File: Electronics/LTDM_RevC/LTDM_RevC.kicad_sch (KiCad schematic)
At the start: 182 parts, among them J1 Conn_01x03_Male, J11 CSR_Bypass, J12 SpringTerminal, J13 Ban1, J14 CSR_Bypass, J15 SpringTerminal, J16 Barrel_Jack, J17 Ban2, J18 Conn_01x03_Male, J2 Conn_01x03_Male, J22 Barrel_Jack, J25 Ban3, J26 Conn_01x03_Male, J29 Conn_01x03_Male, J31 Conn_01x03_Male, J32 Conn_01x03_Male, J4 Conn_01x03_Male, J5 Conn_02x15_Odd_Even, J6 Conn_01x03_Male, J7 Conn_01x04_Socket, J9 Conn_01x03_Male, Q5 FQP27P06, Q6 IRLZ44N, SW3 SW_DPST, U1 74LVC1G11, U10 AP64501SP, U15 LM393, U17 OPA2350, U20 74AUC2G86, U26 74LVC1G11, U3 OPA2350, U31 74LVC1G11, U32 74LVC1G11, U5 LM393, U7 Teensy4.1A, U8 Teensy4.1B

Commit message: Improved  and characterized ADC sample time
Previously took ~6.3uS to sample both ADCs but have gotten it down to a sweet ~3.4uS by disabling 'long sampling mode' and ADC_CFG_ADSTS(3) to ADC_CFG_ADSTS(0). Apparently that was upping sample time.

This arrangement is likely noisier but gives a user an extra 3.5uS to play with in render()

This is for 600MHz.

Trimming away old code too :)
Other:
- sheet String_Drivers_GD1 ports: added STRING1-; removed STRING-
- note removed: "Improvements to Rev B boards: ☑ Change OPA350 to OPA2350 - now has correct pinout and is slightly cheaper ☑ Fixed polarity of dc barrel jacks ☑ Reverse polarity protection(!!) ☑ Rearrange pinout to use FlexPWM output directly (going to have to perform some surgery on current board to verify a correct pinout). -On that note, add a dev board style pinheader breakout to give access to unused pins. W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"
- note removed: "change log: -removed connection between Pin 2<->9 and 3<->10 -- 9 & 10 were hardware interrupts, but changed to use software interrupts - preamplifier used to have balanced gain of 22.28 per stage for total of ~496, but now the first stage has more gain and the second less - to incorporate the S+H and have a slightly hotter output from the S+H -5V regulator - is switch-controlled rather than jump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"
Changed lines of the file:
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@@
 	(text "Ongoing questions:\n- reconsidering the idea of shunting the current out of the resistor"
 		(exclude_from_sim no)
-		(at -37.084 -11.176 0)
+		(at 11.43 7.112 0)
 		(effects
 			(font
@@
 		)
 	)
-	(text "change log:\n\n-removed connection between Pin 2<->9 and 3<->10 -- 9 & 10 were hardware interrupts, but changed to use software interrupts\n\n- preamplifier used to have balanced gain of 22.28 per stage for total of ~496, but now the first stage has more gain and the second less\n	- to incorporate the S+H and have a slightly hotter output from the S+H\n\n-5V regulator\n	- is switch-controlled rather than jumper controlled\n	- higher performance buck converter rather linear 7805\n\n- dissipating resistor changed from  680Ohm (1/4W) to 100Ohm (5W). Better dissipation of ringing.\n\n- Removed potentiometers from precision rectifiers - instead relying on 0.1% thin film resistors"
-		(exclude_from_sim no)
-		(at 181.864 -17.526 0)
-		(effects
-			(font
-				(size 1.27 1.27)
-			)
-			(justify left)
-		)
-	)
 	(text "Key:\nSW = switch (8)\nBT = button (8)\nFP = footpedal (2)\nSL = Slide Pot (8)\nRV = potentiometer (8)"
 		(exclude_from_sim no)
@@
 		)
 	)
-	(text "Improvements to Rev B boards:\n☑ Change OPA350 to OPA2350 - now has correct pinout and is slightly cheaper\n☑ Fixed polarity of dc barrel jacks\n☑ Reverse polarity protection(!!)\n☑ Rearrange pinout to use FlexPWM output directly (going to have to perform some surgery on current board to verify a correct pinout).\n-On that note, add a dev board style pinheader breakout to give access to unused pins. Will be nice if I try to do any LED aliasing experiments --> NVM - using most pins already :)\n-move onboard 5V regulator jumper - too hard to reach currently when switching between teensy power over USB vs powered by 12V supply  (maybe replace with a small switch??)\n-mounting holes for Heat sink leads. (Planning to only use the TO-220-2 package resistors now bc of easy value swapping and easy heatsinking)\n☑ PCB mount 1/4” TRS Expression Pedal plugs (at least two). Maybe panel mount instead incase we want to make an enclosure for this board.\n\nStretch goals, though this might be getting beyond “just a few minor changes”\n-add an FX insert between string sense and teensy analog in for experimenting with pedals in the loop. Nice linear buffered output and input.\n-Small current-sense resistor before string is terminated to ground for measuring current with scope. Will be nice for string comparison analysis.\n-Add sample-and-hold (need to figure out the most appropriate spot for this), but this will be necessary for FX send/return anyway. Makes it possible to monitor/record/listen/add effects to a direct audio output rather than just relying on microphone, acoustic output, or piezo pickups. I’m very interested to hear what this sounds like and if it can be used to sound good.\n-Move analog switch - it needs to be able to switch the analogRead()’s input to come pre or post FX insert. This would be so we can switch between active sustaining with FX and active damping.\n-Adjustable string sense input gain with a trim pot might be nice - we’re occasionally clipping the input when a string really gets moving hard or we use stronger magnets.\n-Any leftover GPIO would be nice to throw some DIP switches or tactile buttons to for further devboard-iness\n-Add a current sense bit\n- Shift S&H to go between gain blocks"
-		(exclude_from_sim no)
-		(at 22.86 -62.23 0)
-		(effects
-			(font
-				(size 1.27 1.27)
-			)
-			(justify left)
-		)
-	)
 	(text "Excluding these because the true gate drivers are better (I think...)\nProperties:\n[X] Exclude from board (to exclude from board)\n[X] Do not populate (for the visual)\n\ncould be cheaper alternative to proper gate drivers"
 		(exclude_from_sim no)
@@
 		)
 		(instances
-			(project "Lorentz_TDM_RevB_V2"
+			(project "LTDM_RevC"
 				(path "/21bd285d-c5a5-466d-bf8a-edfa6cbb8182"
 					(page "7")
@@
 		)
 		(instances
-			(project "Lorentz_TDM_RevB_V2"
+			(project "LTDM_RevC"
 				(path "/21bd285d-c5a5-466d-bf8a-edfa6cbb8182"
 					(page "7")
@@
 			)
 		)
-		(pin "STRING-" output
+		(pin "STRING1-" output
 			(at 511.81 120.65 0)
 			(effects
@@
 		)
 		(instances
-			(project "Lorentz_TDM_RevB_V2"
+			(project "LTDM_RevC"
 				(path "/21bd285d-c5a5-466d-bf8a-edfa6cbb8182"
 					(page "8")
@@
 		)
 		(instances
-			(project "Lorentz_TDM_RevB_V2"
+			(project "LTDM_RevC"
 				(path "/21bd285d-c5a5-466d-bf8a-edfa6cbb8182"
 					(page "6")
@@
 		)
 		(instances
-			(project "Lorentz_TDM_RevB_V2"
+			(project "LTDM_RevC"
 				(path "/21bd285d-c5a5-466d-bf8a-edfa6cbb8182"
 					(page "3")
@@
 		)
 		(instances
-			(project "Lorentz_TDM_RevB_V2"
+			(project "LTDM_RevC"
 				(path "/21bd285d-c5a5-466d-bf8a-edfa6cbb8182"
 					(page "2")
@@
 		)
 		(instances
-			(project "Lorentz_TDM_RevB_V2"
+			(project "LTDM_RevC"
 				(path "/21bd285d-c5a5-466d-bf8a-edfa6cbb8182"
 					(page "5")

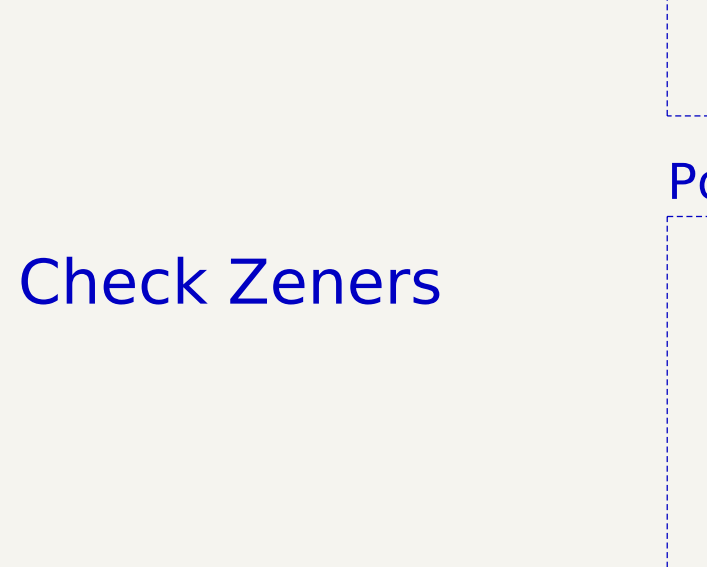
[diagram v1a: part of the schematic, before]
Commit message: Channel 2 fixed!
Channel 2 now working again
Now you can enable/disable RMS limiting and noise
LEDs indicate settings (refer to visualguide.jpg)
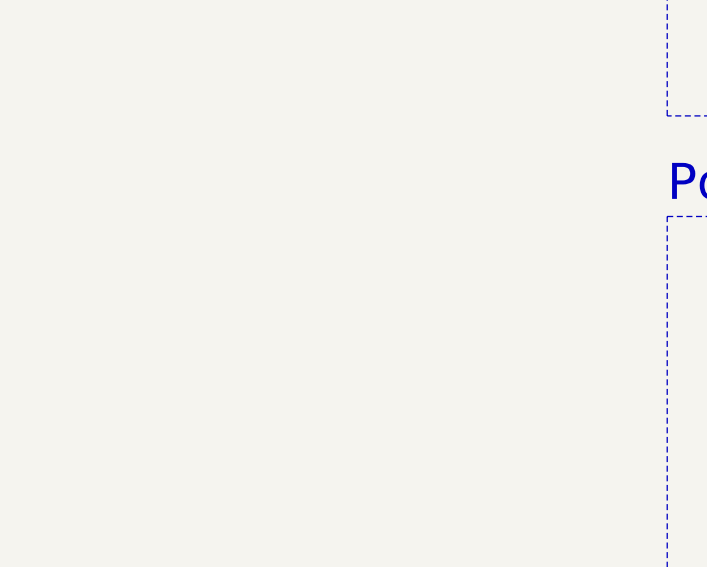
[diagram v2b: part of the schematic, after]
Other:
- note removed: "Check Zeners"
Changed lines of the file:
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@@
 		)
 	)
-	(text "Check Zeners"
-		(exclude_from_sim no)
-		(at -56.896 299.466 0)
-		(effects
-			(font
-				(size 5 5)
-			)
-			(justify left)
-		)
-	)
 	(text "-12V Jack"
 		(exclude_from_sim no)
@@
 	)
 	(image
-		(at 828.04 180.34)
+		(at 850.9 170.18)
 		(data "iVBORw0KGgoAAAANSUhEUgAAA7oAAASOCAYAAADrSFBYAAAMTGlDQ1BJQ0MgUHJvZmlsZQAASImV"
 			"VwdYU8kWnltSIQQIREBK6E0QkRJASggtgPQiiEpIAoQSY0JQsaOLCq5dRLCiqyCKHRCxYVcWxe5a"

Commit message: Boards Ordered!
The KiCad files are the ones that were ordered
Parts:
- removed C21: 100n, Capacitor_SMD:C_0402_1005Metric, symbol Device:C
- removed C47: 220u, Capacitor_THT:CP_Radial_D8.0mm_P3.50mm, symbol Device:C_Polarized
- removed J26, J4: Conn_01x03_Male, Connector_PinHeader_2.54mm:PinHeader_1x03_P2.54mm_Vertical, symbol Connector:Conn_01x03_Male
- removed R10, R61: 2.7k, Resistor_SMD:R_0603_1608Metric, symbol 1A_Favorites:R_0603_SMD
- removed R16, R22: 10k, Resistor_SMD:R_0603_1608Metric, symbol 1A_Favorites:R_0603_SMD
- removed R55: 1k, Resistor_SMD:R_0603_1608Metric, symbol 1A_Favorites:R_0603_SMD
- added CU49, CU50, CU51, CU52, CU53: 100n, Capacitor_SMD:C_0603_1608Metric, symbol 1A_Favorites:C_0603_SMD
- added J23: Conn_01x03_Male, Connector_PinHeader_2.54mm:PinHeader_1x03_P2.54mm_Vertical, symbol Connector:Conn_01x03_Male
- added J4: Conn_02x05_Odd_Even, Connector_PinHeader_2.54mm:PinHeader_2x05_P2.54mm_Vertical, symbol Connector_Generic:Conn_02x05_Odd_Even
- added Q15, Q16: BSS123, Package_TO_SOT_SMD:SOT-23, symbol Transistor_FET:BSS123
- added R10, R142, R16, R22, R55, R61: 10k, Resistor_SMD:R_0603_1608Metric, symbol 1A_Favorites:R_Standard_Thru
- added R136: 2.2k, Resistor_SMD:R_0603_1608Metric, symbol Device:R_US
- added R137, R139: 1k, Resistor_SMD:R_0603_1608Metric, symbol 1A_Favorites:R_0603_SMD
- added R138: 1Meg, Resistor_SMD:R_0603_1608Metric, symbol 1A_Favorites:R_0603_SMD
- added R140, R141: 4.7k, Resistor_SMD:R_0603_1608Metric, symbol 1A_Favorites:R_0603_SMD
- added R143: 10k, Resistor_SMD:R_0603_1608Metric, symbol 1A_Favorites:R_0603_SMD
- added R144: 176K, Resistor_SMD:R_0402_1005Metric, symbol Device:R_US
- added RV1: 1k, Potentiometer_SMD:Potentiometer_Bourns_3314G_Vertical, symbol Device:R_Potentiometer_US
- added TP45, TP46, TP47, TP48, TP49: TestPoint, TestPoint:TestPoint_THTPad_D2.0mm_Drill1.0mm, symbol Connector:TestPoint
- added U30: OPA1612AxD, Package_SO:SOP-8_3.76x4.96mm_P1.27mm, symbol Amplifier_Operational:OPA1612AxD
- added U36: 74LVC2G74, Package_SO:VSSOP-8_2.3x2mm_P0.5mm, symbol 74xGxx:74LVC2G74
- R26, R40: value 100R 5W -> 100R 1W; footprint Resistor_SMD:R_13.5x7.3mm -> Resistor_SMD:R_2512_6332Metric; LCSC C6489070 -> C24920
- R41, R48: LCSC (none) -> C309660
- R7: value 1k -> 100k
- TP18, TP20, TP22, TP23, TP26, TP27, TP28, TP29, TP30, TP5, TP7, TP8: LCSC C238122 -> C238127
- U10: value AP64501SP -> AP64500SP; LCSC C2071517 -> C2070920
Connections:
- net +12V: now also CU49.1, U30.8 (V+); no longer J32.3 (Pin_3), R15.2, R67.2
- net +3.3V: now also R15.2, R67.2, CU52.1, J4.7 (Pin_7), J4.8 (Pin_8), R136.1, R139.2, U36.2 (D), U36.7 (~{PRE}), U36.8 (VCC)
- net +5V: now also J32.2 (Pin_2), CU50.1, J23.1 (Pin_1), J4.10 (Pin_10), J4.9 (Pin_9)
- net -12V: now also CU53.2, U30.4 (V-)
- net CH1_Enable: now also R141.2; no longer U1.3, U26.1
- net CH2_Enable: now also R140.2; no longer U31.3, U32.1
- net GND: now also CU49.2, CU50.2, CU51.2, CU52.2, CU53.1, J23.2 (Pin_2), J4.1 (Pin_1), J4.2 (Pin_2), Q15.2 (S), Q16.2 (S), R143.1, R144.2, RV1.3, TP49.1, U36.4 (GND)
- net N_Drive1: now also R55.2; no longer R128.2
- net N_Drive2: now also R16.2
- net P_Drive1: now also R61.2; no longer R129.2
- net P_Drive2: now also R10.2
- net SignIn1: now also R15.1, R6.2, U5.1; no longer R7.2
- net SignIn2: now also R54.2, R67.1, U15.1
- net Temp_Out: now reaches U5.6 (-)
- net Temp_Out: now also R7.2, U8.43 (21_A7_RX5_BCLK1), CU51.1, J23.3 (Pin_3), TP46.1
- net at U5.5 (+): now also R137.2, R138.1
- net at U10.4 (SS): now also R144.1
- net at U5.7: now also R138.2, R139.1, U36.6 (~{CLR})
- net GPIO0: now reaches U7.2 (0_RX1_CRX2_CS1)
- net GPIO0: now also J4.3 (Pin_3)
- net GPIO1: now reaches U7.3 (1_TX1_CTX2_MISO1)
- net GPIO1: now also J4.5 (Pin_5)
- net Temp_Reset: now reaches U7.9 (7_RX2_OUT1A)
- net Temp_Reset: now also R143.2, U36.1 (C)
- net GPIO17/A3: now reaches U8.39 (17_A3_TX4_SDA1)
- net GPIO17/A3: now also J4.6 (Pin_6)
- net GPIO20/A6: now reaches U8.42 (20_A6_TX5_LRCLK1)
- net GPIO20/A6: now also J4.4 (Pin_4)
- net LED_3 renamed SERVO
- net SERVO: now also J32.3 (Pin_3); no longer J32.2 (Pin_2)
- new net: R16.1, R22.2, U30.2 (-)
- new net: R136.2, RV1.1
- new net: R129.2, R61.1, U30.5 (+)
- new net: R142.2, R55.1, U30.6 (-)
- new net: R10.1, R128.2, U30.3 (+)
- new net CH1_Enable_GATE: Q16.3 (D), R141.1, U1.3, U26.1
- new net CH2_Enable_GATE: Q15.3 (D), R140.1, U31.3, U32.1
- new net Drive1_Preview: R142.1, TP48.1, U30.7
- new net Drive2_Preview: R22.1, TP47.1, U30.1
- new net Temp_Fault: Q15.1 (G), Q16.1 (G), U36.3 (~{Q})
- new net Temp_Thresh: R137.1, RV1.2, TP45.1
- no-connect marks 6 -> 8
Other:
- note added: "- verify which pin is available for thermal reset"
- note added: "-Temp_fault HIGH when temperature exceeded -Causes BSS123 to conduct, pulling CH1_Enable and CH2 both LOW"
- note added: "If Temp_sense signal exceeds Temp_thresh, comparator output goes LOW Comparator output low into ~{CLR} forces Q LOW Temp_Reset rising edge passes D to Q, putting it high again"
- note added: "LM35 TO-220 temp sensor connector"
- note added: "LM35 TO-220 temp sensor connector https://docs.rs-online.com/abdd/A700000006857169.pdf"
- note added: "Preview actuation output with one pin"
- note added: "Previously used the AP64501SP - in that case, SS needs to be connnected to 100nF cap For this, SS pin is actually 'RT' and controls clock rate"
- note added: "R7 pulls temp reading to GND when no sensor connected"
- note added: "Thermal Shutdown"
- note added: "expecting to set threshold to 45-55ºC = 0.45V-0.55V 3.3V*1K/(2.2K+1K) = 1.03V max threshold seems reasonable ... circuit trips at ~0.5V when pot is set to halfway for a future version, bringing these resistor values to reduce power consumption would be better ..."
- moved on the sheet: C11, C12, C13, C14, C15, C16, C17, C18, C19, C20, C22, C23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
